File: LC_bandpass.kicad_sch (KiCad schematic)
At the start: 3 parts

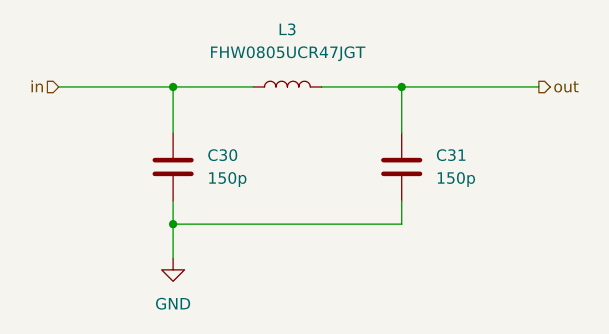
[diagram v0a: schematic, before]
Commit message: Version 1.0 submitted to JLCPCB
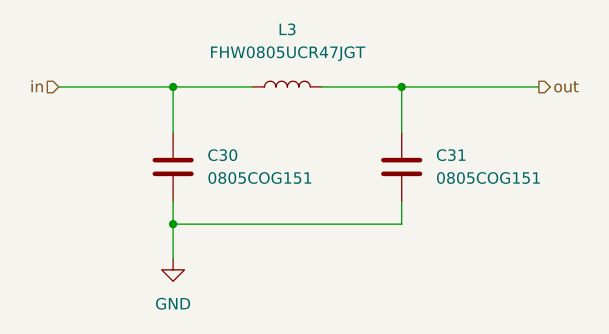
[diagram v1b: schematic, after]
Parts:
- C30, C31: value 150p -> 0805COG151
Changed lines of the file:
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@@
       (effects (font (size 1.27 1.27)) (justify right))
     )
-    (property "Value" "150p" (id 1) (at 157.48 99.0599 0)
+    (property "Value" "0805COG151" (id 1) (at 157.48 99.0599 0)
       (effects (font (size 1.27 1.27)) (justify right))
     )
@@
       (effects (font (size 1.27 1.27)) (justify right))
     )
-    (property "Value" "150p" (id 1) (at 132.08 99.0599 0)
+    (property "Value" "0805COG151" (id 1) (at 132.08 99.0599 0)
       (effects (font (size 1.27 1.27)) (justify right))
     )
